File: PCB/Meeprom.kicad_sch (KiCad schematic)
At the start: 3 parts, among them J1 Molex 78805 socket with 27C25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, U1 28C256 / FM18W08

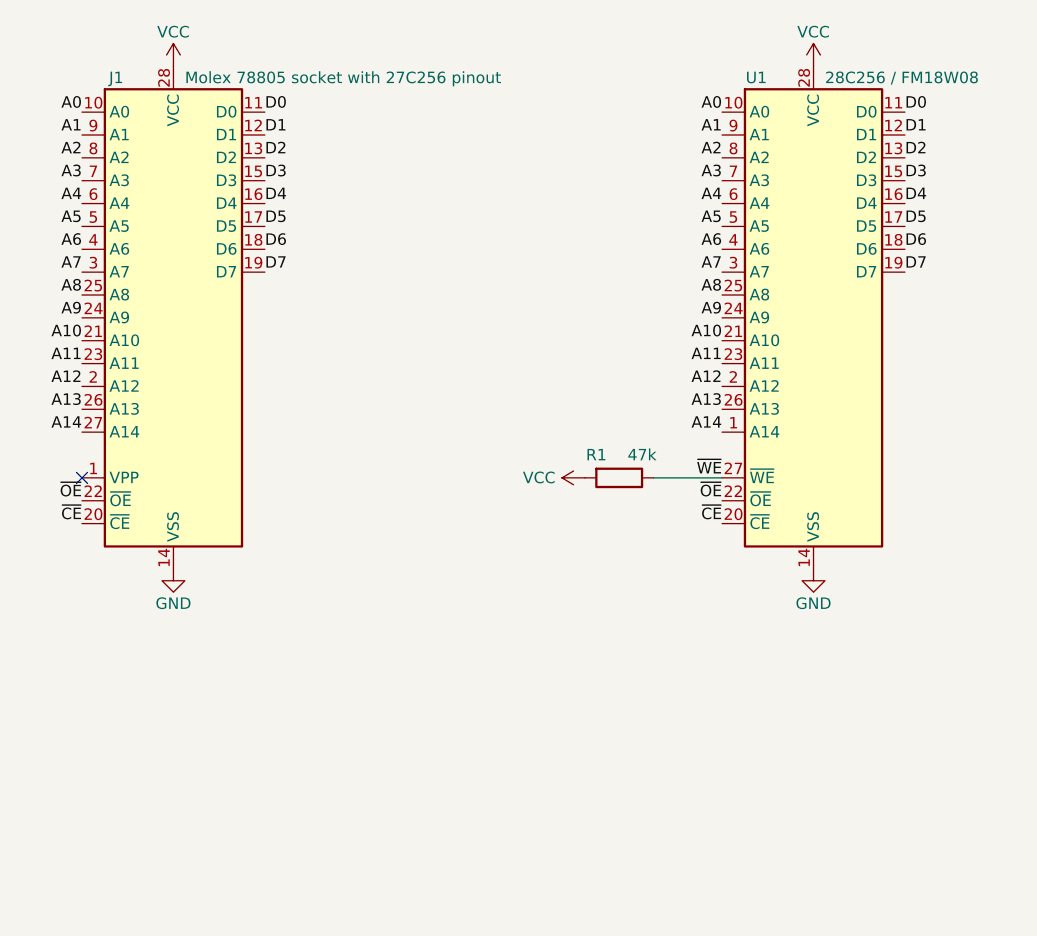
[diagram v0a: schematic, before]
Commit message: add caps & fiducials, remove dead shapeways links
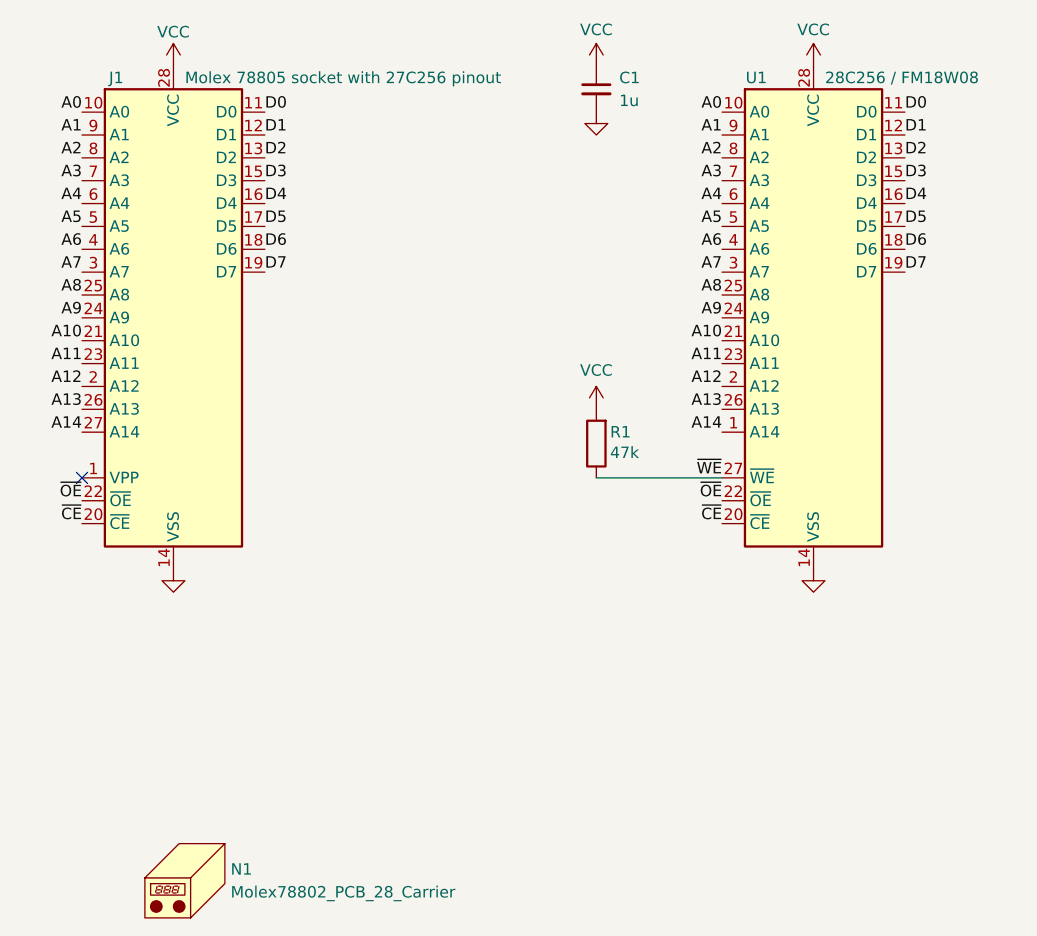
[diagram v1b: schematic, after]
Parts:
- added C1: 1u, 000_LOCAL:C_0805, symbol 000_LOCAL:C
- added N1: Molex78802_PCB_28_Carrier, 000_LOCAL:Molex78802_PCB_28_Carrier, symbol 000_LOCAL:Housing
- J1: now left out of the parts list
- U1: MPN (none) -> AT28C256-15SU
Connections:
- net GND: now also C1.2
- net VCC: now also C1.1
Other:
- moved on the sheet: R1

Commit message: bom
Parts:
- R1: MPN (none) -> CRCW080547K0FKEA
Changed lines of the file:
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@@
 	(title_block
 		(title "Meeprom-28")
-		(date "2022-12-21")
+		(date "2026-02-23")
 		(rev "005")
 		(comment 3 "28C256 to Molex 78805 socket with 27C256 pinout")
@@
 		(dnp no)
 		(property "Reference" "R1"
-			(at 160.274 102.87 0)
+			(at 160.528 102.87 0)
 			(effects
 				(font
@@
 		)
 		(property "Value" "47k"
-			(at 160.274 105.156 0)
+			(at 160.274 105.41 0)
 			(effects
 				(font
@@
 			)
 		)
-		(property "Datasheet" "~"
+		(property "Datasheet" "datasheets/dcrcwe3.pdf"
 			(at 158.75 104.14 0)
 			(effects
@@
 			)
 		)
-		(property "Description" ""
+		(property "Description" "R 47K 1% 0.25W 0805"
+			(at 158.75 93.726 0)
+			(effects
+				(font
+					(size 1.27 1.27)
+				)
+				(hide yes)
+			)
+		)
+		(property "MPN" "CRCW080547K0FKEA"
 			(at 158.75 104.14 0)
 			(effects
@@
 					(size 1.27 1.27)
 				)
+				(hide yes)
 			)
 		)
@@
 		(at 114.3 152.4 0)
 		(unit 1)
-		(exclude_from_sim no)
+		(exclude_from_sim yes)
 		(in_bom no)
 		(on_board yes)
